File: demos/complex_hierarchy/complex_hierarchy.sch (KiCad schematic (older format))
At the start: 10 parts, among them P1 CONN_2, P2 CONN_2, U1 ICL7660, U2 78L05

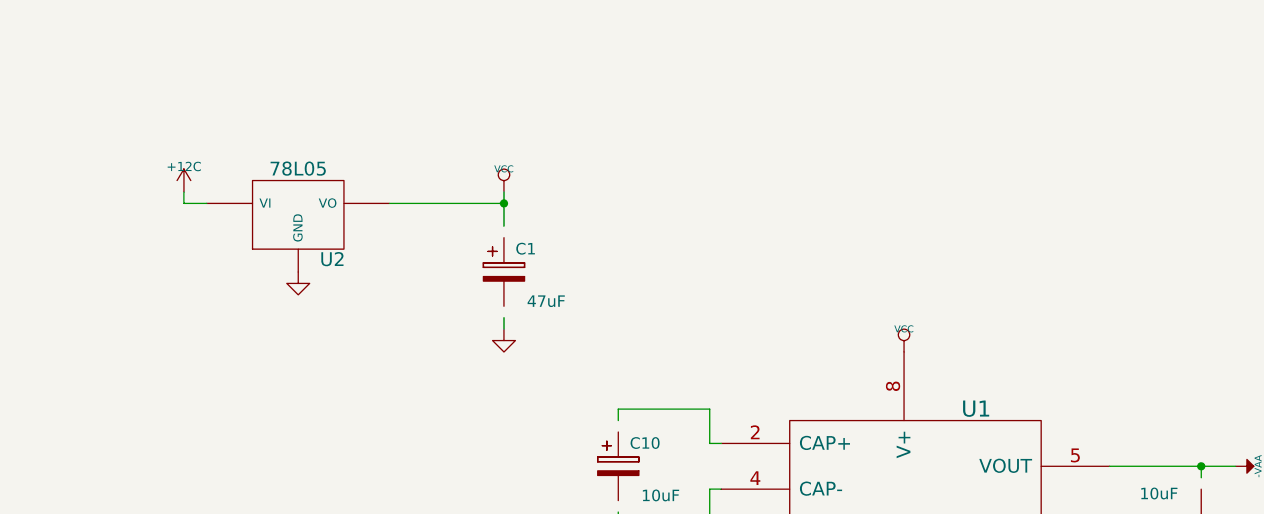
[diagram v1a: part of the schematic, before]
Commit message: Update demo files. A minor code cleaning.
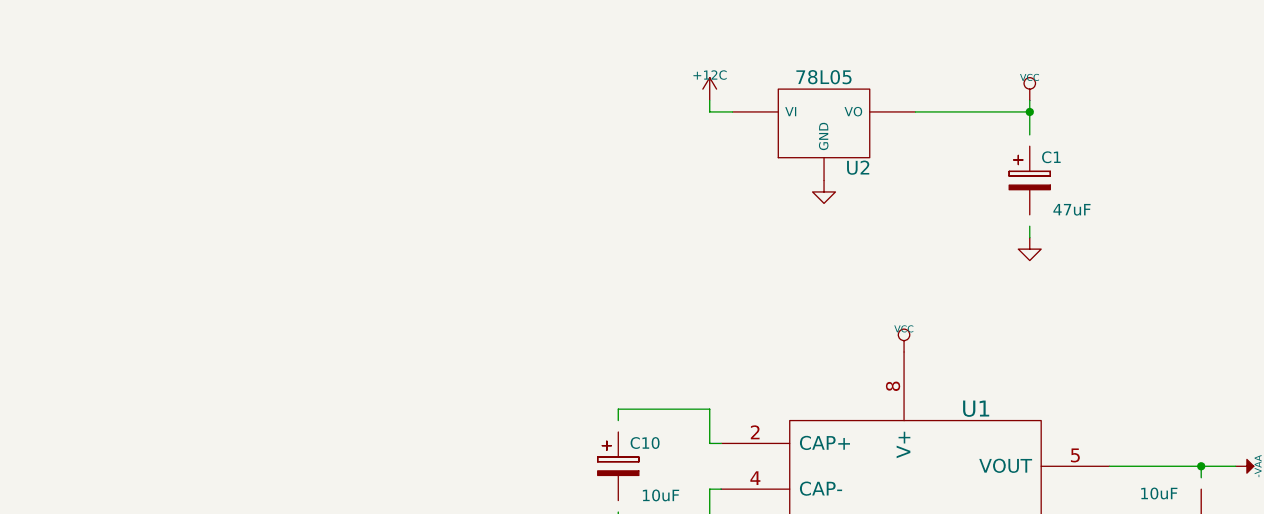
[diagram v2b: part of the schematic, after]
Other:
- moved on the sheet: C1, U2

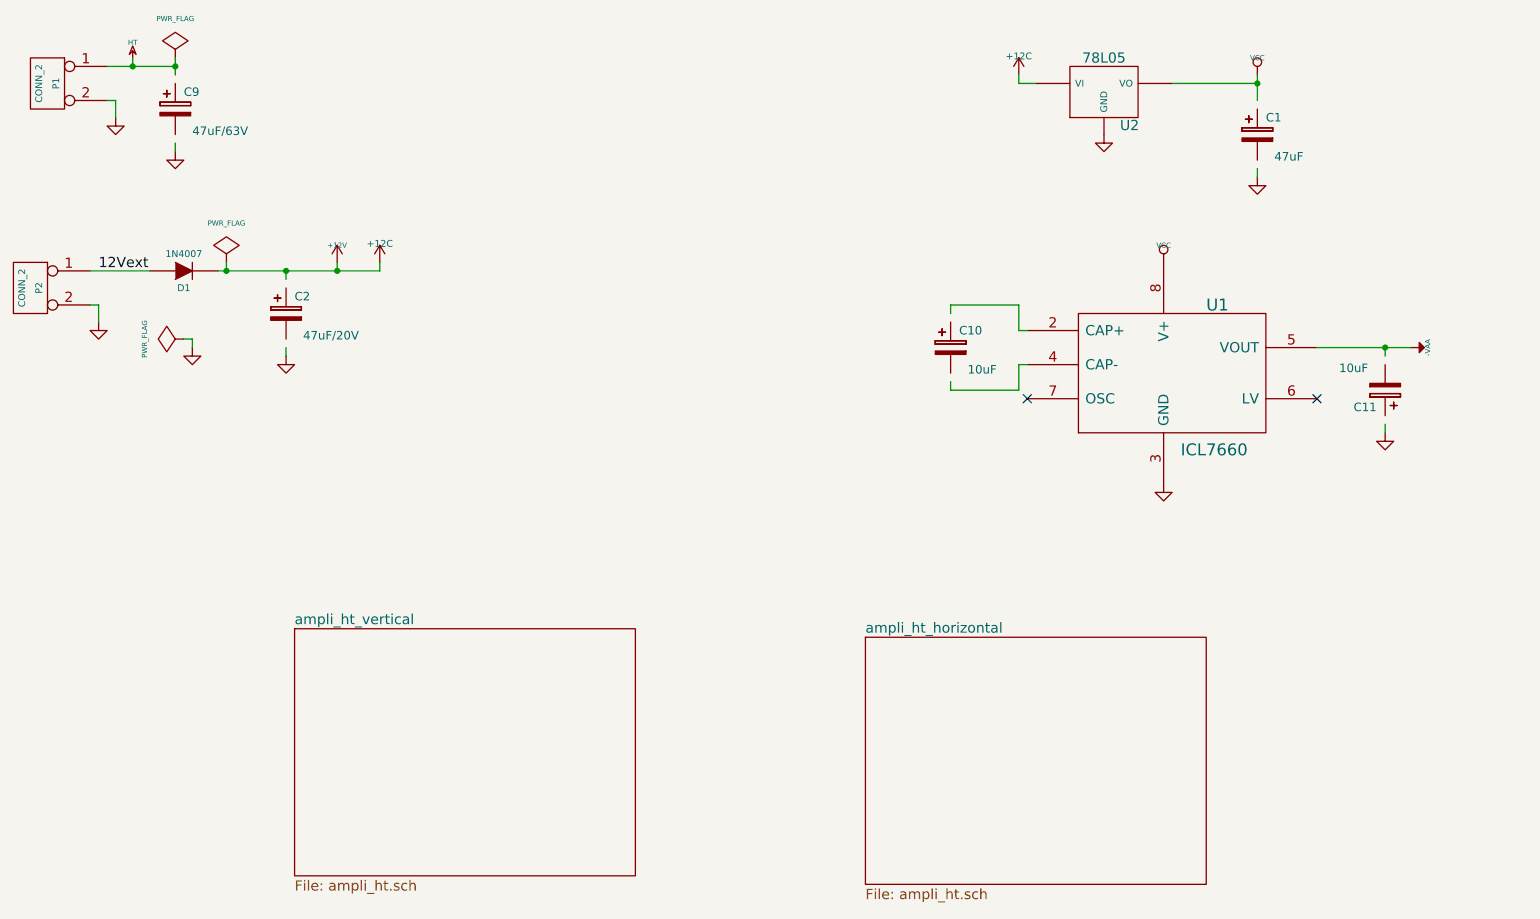
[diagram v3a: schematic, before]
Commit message: demos/ schematic tidying
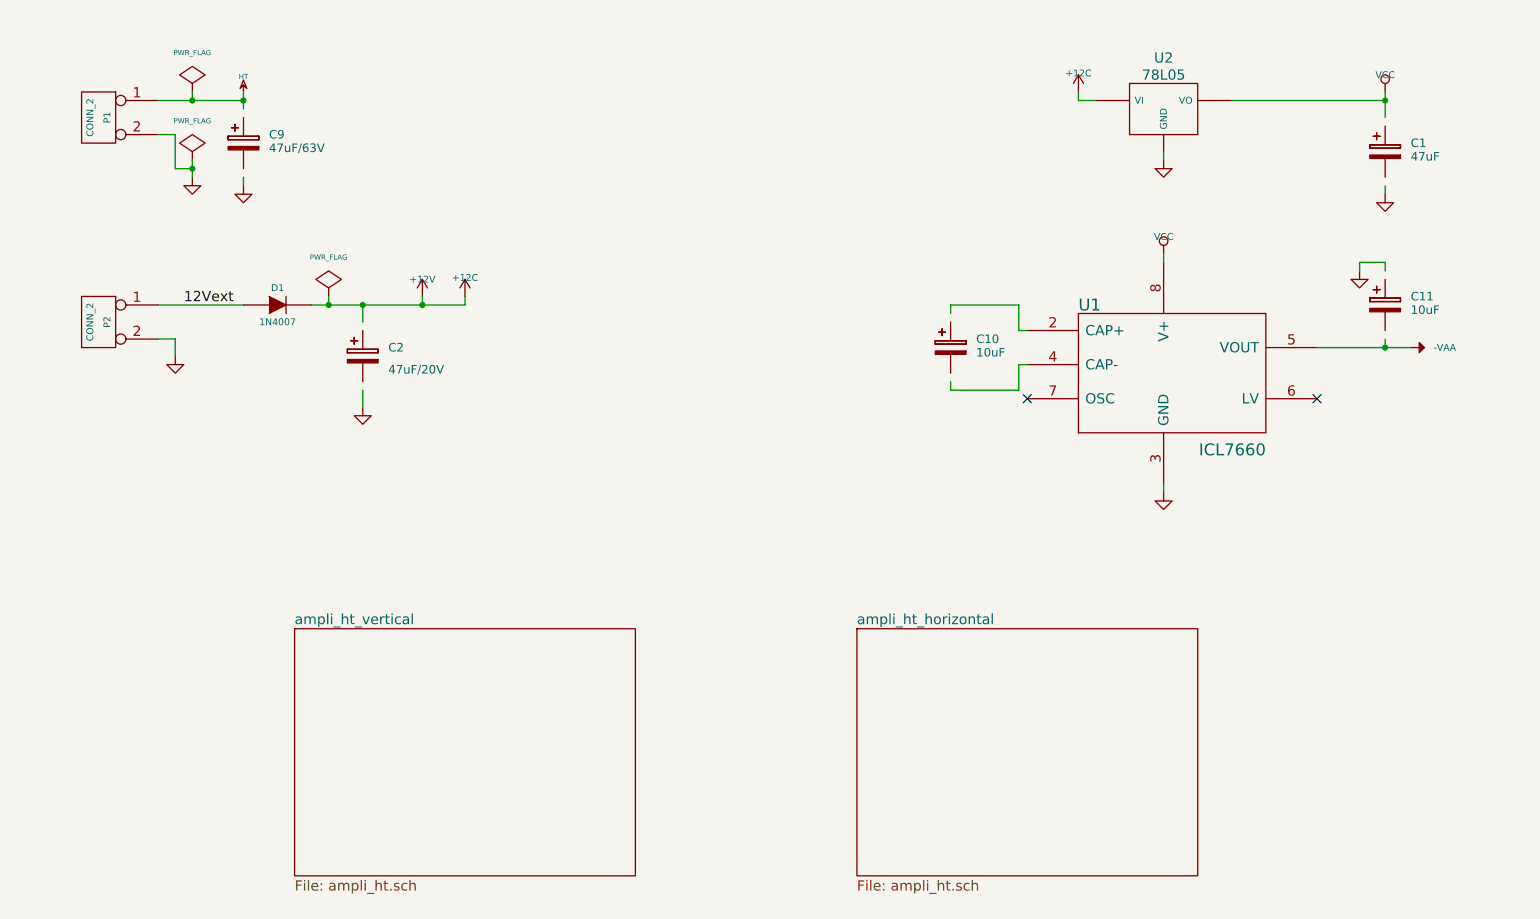
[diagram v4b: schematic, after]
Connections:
- wire segments 33 -> 38
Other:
- moved on the sheet: C1, C11, C2, C9, D1, P1, P2, U2

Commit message: Eeschema: BOM dialog: fix some minor issues when displaying messages. Cvpcb: fix Bug #1470201 (select next/previous unlinked comp and clear links not working well) demo/complex_hierarchy: use our new schematic symbols.
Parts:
- C1, C10, C11, C2: footprint (none) -> discret:CP6
- C9: footprint (none) -> discret:CP8
- D1: footprint (none) -> discret:D5; symbol DIODE -> D_Small
- P1, P2: footprint (none) -> connect:bornier2
- U1: footprint (none) -> dip_sockets:DIP-8__300_ELL
- U2: footprint (none) -> discret:LM78LXX
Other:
- moved on the sheet: C2, C9
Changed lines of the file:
@@
 EESchema Schematic File Version 2
-LIBS:complex_hierarchy_schlib
+LIBS:device
 LIBS:power
 LIBS:complex_hierarchy-cache
@@
 Connection ~ 9200 2750
 Wire Wire Line
-	9200 2700 9200 2750
-Wire Wire Line
-	6650 2950 6650 3000
+	9200 2650 9200 2750
+Wire Wire Line
+	6650 2900 6650 3000
 Wire Wire Line
 	6650 3000 7050 3000
@@
 	7050 2850 7100 2850
 Wire Wire Line
-	9200 2300 9200 2250
+	9200 2350 9200 2250
 Connection ~ 2500 1300
 Wire Wire Line
 	8300 1300 9200 1300
 Wire Wire Line
-	2900 2500 3800 2500
+	2800 2500 3800 2500
 Wire Wire Line
 	2500 1250 2500 1350
@@
 	2100 2700 2000 2700
 Wire Wire Line
-	2000 2500 2500 2500
-Wire Wire Line
-	3200 3000 3200 3100
+	2000 2500 2600 2500
+Wire Wire Line
+	3200 2900 3200 3000
 Wire Wire Line
 	3200 2500 3200 2600
@@
 	7400 1300 7500 1300
 Wire Wire Line
-	9200 1800 9200 1850
-Wire Wire Line
-	9200 1250 9200 1400
+	9200 1750 9200 1800
+Wire Wire Line
+	9200 1250 9200 1450
 Connection ~ 9200 1300
 Wire Wire Line
 	2200 1650 2200 1750
 Wire Wire Line
-	2500 1750 2500 1800
-Wire Wire Line
-	6650 2550 6650 2500
+	2500 1650 2500 1700
+Wire Wire Line
+	6650 2600 6650 2500
 Wire Wire Line
 	6650 2500 7050 2500
@@
 F 0 "C10" H 6800 2800 50  0000 L CNN
 F 1 "10uF" H 6800 2750 50  0000 L TNN
-F 2 "" H 6650 2750 60  0001 C CNN
+F 2 "discret:CP6" H 6650 2750 60  0001 C CNN
 F 3 "" H 6650 2750 60  0001 C CNN
 	1    6650 2750
@@
 F 0 "C11" H 9350 2550 50  0000 L CNN
 F 1 "10uF" H 9350 2500 50  0000 L TNN
-F 2 "" H 9200 2500 60  0001 C CNN
+F 2 "discret:CP6" H 9200 2500 60  0001 C CNN
 F 3 "" H 9200 2500 60  0001 C CNN
 	1    9200 2500
@@
 F 0 "U2" H 7900 1650 60  0000 C CNN
 F 1 "78L05" H 7900 1550 60  0000 C CNN
-F 2 "" H 7900 1350 60  0001 C CNN
+F 2 "discret:LM78LXX" H 7900 1350 60  0001 C CNN
 F 3 "" H 7900 1350 60  0001 C CNN
 	1    7900 1350
@@
 F 0 "U1" H 7400 3300 70  0000 L CNN
 F 1 "ICL7660" H 8500 2450 70  0000 R CNN
-F 2 "" H 7950 2900 60  0001 C CNN
+F 2 "dip_sockets:DIP-8__300_ELL" H 7950 2900 60  0001 C CNN
 F 3 "" H 7950 2900 60  0001 C CNN
 	1    7950 2900
@@
 L CP C9
 U 1 1 4B3A1558
-P 2500 1550
-F 0 "C9" H 2650 1600 50  0000 L CNN
-F 1 "47uF/63V" H 2650 1550 50  0000 L TNN
-F 2 "" H 2500 1550 60  0001 C CNN
-F 3 "" H 2500 1550 60  0001 C CNN
-	1    2500 1550
+P 2500 1500
+F 0 "C9" H 2650 1550 50  0000 L CNN
+F 1 "47uF/63V" H 2650 1500 50  0000 L TNN
+F 2 "discret:CP8" H 2500 1500 60  0001 C CNN
+F 3 "" H 2500 1500 60  0001 C CNN
+	1    2500 1500
 	1    0    0    -1
 $EndComp
@@
 L GND #PWR06
 U 1 1 4B3A1557
-P 2500 1800
-F 0 "#PWR06" H 2500 1800 30  0001 C CNN
-F 1 "GND" H 2500 1730 30  0001 C CNN
-F 2 "" H 2500 1800 60  0001 C CNN
-F 3 "" H 2500 1800 60  0001 C CNN
-	1    2500 1800
+P 2500 1700
+F 0 "#PWR06" H 2500 1700 30  0001 C CNN
+F 1 "GND" H 2500 1630 30  0001 C CNN
+F 2 "" H 2500 1700 60  0001 C CNN
+F 3 "" H 2500 1700 60  0001 C CNN
+	1    2500 1700
 	1    0    0    -1
 $EndComp
@@
 F 0 "P1" V 1600 1400 40  0000 C CNN
 F 1 "CONN_2" V 1700 1400 40  0000 C CNN
-F 2 "" H 1650 1400 60  0001 C CNN
+F 2 "connect:bornier2" H 1650 1400 60  0001 C CNN
 F 3 "" H 1650 1400 60  0001 C CNN
 	1    1650 1400
@@
 F 0 "C1" H 9350 1650 50  0000 L CNN
 F 1 "47uF" H 9350 1600 50  0000 L TNN
-F 2 "" H 9200 1600 60  0001 C CNN
+F 2 "discret:CP6" H 9200 1600 60  0001 C CNN
 F 3 "" H 9200 1600 60  0001 C CNN
 	1    9200 1600
@@
 L GND #PWR09
 U 1 1 4B03CEC1
-P 9200 1850
-F 0 "#PWR09" H 9200 1850 30  0001 C CNN
-F 1 "GND" H 9200 1780 30  0001 C CNN
-F 2 "" H 9200 1850 60  0001 C CNN
-F 3 "" H 9200 1850 60  0001 C CNN
-	1    9200 1850
+P 9200 1800
+F 0 "#PWR09" H 9200 1800 30  0001 C CNN
+F 1 "GND" H 9200 1730 30  0001 C CNN
+F 2 "" H 9200 1800 60  0001 C CNN
+F 3 "" H 9200 1800 60  0001 C CNN
+	1    9200 1800
 	1    0    0    -1
 $EndComp
@@
 L GND #PWR017
 U 1 1 4AE173D0
-P 3200 3100
-F 0 "#PWR017" H 3200 3100 30  0001 C CNN
-F 1 "GND" H 3200 3030 30  0001 C CNN
-F 2 "" H 3200 3100 60  0001 C CNN
-F 3 "" H 3200 3100 60  0001 C CNN
-	1    3200 3100
+P 3200 3000
+F 0 "#PWR017" H 3200 3000 30  0001 C CNN
+F 1 "GND" H 3200 2930 30  0001 C CNN
+F 2 "" H 3200 3000 60  0001 C CNN
+F 3 "" H 3200 3000 60  0001 C CNN
+	1    3200 3000
 	1    0    0    -1
 $EndComp
@@
 L CP C2
 U 1 1 4AE173CF
-P 3200 2800
-F 0 "C2" H 3350 2850 50  0000 L CNN
-F 1 "47uF/20V" H 3350 2750 50  0000 L TNN
-F 2 "" H 3200 2800 60  0001 C CNN
-F 3 "" H 3200 2800 60  0001 C CNN
-	1    3200 2800
-	1    0    0    -1
-$EndComp
-$Comp
-L DIODE D1
+P 3200 2750
+F 0 "C2" H 3350 2800 50  0000 L CNN
+F 1 "47uF/20V" H 3350 2700 50  0000 L TNN
+F 2 "discret:CP6" H 3200 2750 60  0001 C CNN
+F 3 "" H 3200 2750 60  0001 C CNN
+	1    3200 2750
+	1    0    0    -1
+$EndComp
+$Comp
+L D_Small D1
 U 1 1 4AE172F4
 P 2700 2500
 F 0 "D1" H 2700 2400 40  0000 C CNN
 F 1 "1N4007" H 2700 2600 40  0000 C CNN
-F 2 "" H 2700 2500 60  0001 C CNN
+F 2 "discret:D5" H 2700 2500 60  0001 C CNN
 F 3 "" H 2700 2500 60  0001 C CNN
 	1    2700 2500
-	1    0    0    1
+	-1   0    0    -1
 $EndComp
 $Comp
@@
 F 0 "P2" V 1600 2600 40  0000 C CNN
 F 1 "CONN_2" V 1700 2600 40  0000 C CNN
-F 2 "" H 1650 2600 60  0001 C CNN
+F 2 "connect:bornier2" H 1650 2600 60  0001 C CNN
 F 3 "" H 1650 2600 60  0001 C CNN
 	1    1650 2600

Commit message: polygons in footprint body: fix incorrect calculation of polygons with clearance or outline thickness (fix bug #1511366) Clean demos
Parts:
- C1, C10, C11, C2: footprint discret:CP6 -> Discret:CP6
- C9: footprint discret:CP8 -> Discret:CP8
- D1: footprint discret:D5 -> Discret:D5
- P1, P2: footprint connect:bornier2 -> Connect:bornier2
- U2: footprint discret:LM78LXX -> Discret:LM78LXX
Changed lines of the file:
@@
 EESchema Schematic File Version 2
-LIBS:device
 LIBS:power
+LIBS:complex_hierarchy_schlib
 LIBS:complex_hierarchy-cache
 EELAYER 25 0
@@
 F 0 "C10" H 6800 2800 50  0000 L CNN
 F 1 "10uF" H 6800 2750 50  0000 L TNN
-F 2 "discret:CP6" H 6650 2750 60  0001 C CNN
+F 2 "Discret:CP6" H 6650 2750 60  0001 C CNN
 F 3 "" H 6650 2750 60  0001 C CNN
 	1    6650 2750
@@
 F 0 "C11" H 9350 2550 50  0000 L CNN
 F 1 "10uF" H 9350 2500 50  0000 L TNN
-F 2 "discret:CP6" H 9200 2500 60  0001 C CNN
+F 2 "Discret:CP6" H 9200 2500 60  0001 C CNN
 F 3 "" H 9200 2500 60  0001 C CNN
 	1    9200 2500
@@
 F 0 "U2" H 7900 1650 60  0000 C CNN
 F 1 "78L05" H 7900 1550 60  0000 C CNN
-F 2 "discret:LM78LXX" H 7900 1350 60  0001 C CNN
+F 2 "Discret:LM78LXX" H 7900 1350 60  0001 C CNN
 F 3 "" H 7900 1350 60  0001 C CNN
 	1    7900 1350
@@
 F 0 "C9" H 2650 1550 50  0000 L CNN
 F 1 "47uF/63V" H 2650 1500 50  0000 L TNN
-F 2 "discret:CP8" H 2500 1500 60  0001 C CNN
+F 2 "Discret:CP8" H 2500 1500 60  0001 C CNN
 F 3 "" H 2500 1500 60  0001 C CNN
 	1    2500 1500
@@
 F 0 "P1" V 1600 1400 40  0000 C CNN
 F 1 "CONN_2" V 1700 1400 40  0000 C CNN
-F 2 "connect:bornier2" H 1650 1400 60  0001 C CNN
+F 2 "Connect:bornier2" H 1650 1400 60  0001 C CNN
 F 3 "" H 1650 1400 60  0001 C CNN
 	1    1650 1400
@@
 F 0 "C1" H 9350 1650 50  0000 L CNN
 F 1 "47uF" H 9350 1600 50  0000 L TNN
-F 2 "discret:CP6" H 9200 1600 60  0001 C CNN
+F 2 "Discret:CP6" H 9200 1600 60  0001 C CNN
 F 3 "" H 9200 1600 60  0001 C CNN
 	1    9200 1600
@@
 F 0 "C2" H 3350 2800 50  0000 L CNN
 F 1 "47uF/20V" H 3350 2700 50  0000 L TNN
-F 2 "discret:CP6" H 3200 2750 60  0001 C CNN
+F 2 "Discret:CP6" H 3200 2750 60  0001 C CNN
 F 3 "" H 3200 2750 60  0001 C CNN
 	1    3200 2750
@@
 F 0 "D1" H 2700 2400 40  0000 C CNN
 F 1 "1N4007" H 2700 2600 40  0000 C CNN
-F 2 "discret:D5" H 2700 2500 60  0001 C CNN
+F 2 "Discret:D5" H 2700 2500 60  0001 C CNN
 F 3 "" H 2700 2500 60  0001 C CNN
 	1    2700 2500
@@
 F 0 "P2" V 1600 2600 40  0000 C CNN
 F 1 "CONN_2" V 1700 2600 40  0000 C CNN
-F 2 "connect:bornier2" H 1650 2600 60  0001 C CNN
+F 2 "Connect:bornier2" H 1650 2600 60  0001 C CNN
 F 3 "" H 1650 2600 60  0001 C CNN
 	1    1650 2600

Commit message: merge from production git:004ca3c 16.01.2017
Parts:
- U1: footprint dip_sockets:DIP-8__300_ELL -> Housings_DIP:DIP-8_W7.62mm_LongPads
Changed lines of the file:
@@
 LIBS:complex_hierarchy_schlib
 LIBS:complex_hierarchy-cache
-EELAYER 25 0
+EELAYER 26 0
 EELAYER END
 $Descr A4 11693 8268
 encoding utf-8
 Sheet 1 3
-Title ""
-Date "21 mar 2015"
+Title "Complex hierarchy: demo"
+Date "2017-01-15"
 Rev ""
 Comp ""
@@
 F 0 "C10" H 6800 2800 50  0000 L CNN
 F 1 "10uF" H 6800 2750 50  0000 L TNN
-F 2 "Discret:CP6" H 6650 2750 60  0001 C CNN
+F 2 "Discret:CP6" H 6850 2650 30  0000 C CNN
 F 3 "" H 6650 2750 60  0001 C CNN
 	1    6650 2750
@@
 F 0 "C11" H 9350 2550 50  0000 L CNN
 F 1 "10uF" H 9350 2500 50  0000 L TNN
-F 2 "Discret:CP6" H 9200 2500 60  0001 C CNN
+F 2 "Discret:CP6" H 9550 2400 30  0000 C CNN
 F 3 "" H 9200 2500 60  0001 C CNN
 	1    9200 2500
@@
 F 0 "U2" H 7900 1650 60  0000 C CNN
 F 1 "78L05" H 7900 1550 60  0000 C CNN
-F 2 "Discret:LM78LXX" H 7900 1350 60  0001 C CNN
+F 2 "Discret:LM78LXX" H 8100 1150 30  0000 C CNN
 F 3 "" H 7900 1350 60  0001 C CNN
 	1    7900 1350
@@
 F 0 "U1" H 7400 3300 70  0000 L CNN
 F 1 "ICL7660" H 8500 2450 70  0000 R CNN
-F 2 "dip_sockets:DIP-8__300_ELL" H 7950 2900 60  0001 C CNN
+F 2 "Housings_DIP:DIP-8_W7.62mm_LongPads" H 8950 2300 60  0000 C CNN
 F 3 "" H 7950 2900 60  0001 C CNN
 	1    7950 2900
@@
 F 0 "C9" H 2650 1550 50  0000 L CNN
 F 1 "47uF/63V" H 2650 1500 50  0000 L TNN
-F 2 "Discret:CP8" H 2500 1500 60  0001 C CNN
+F 2 "Discret:CP8" H 2800 1400 30  0000 C CNN
 F 3 "" H 2500 1500 60  0001 C CNN
 	1    2500 1500
@@
 F 0 "P1" V 1600 1400 40  0000 C CNN
 F 1 "CONN_2" V 1700 1400 40  0000 C CNN
-F 2 "Connect:bornier2" H 1650 1400 60  0001 C CNN
+F 2 "Connect:bornier2" H 1650 1200 30  0000 C CNN
 F 3 "" H 1650 1400 60  0001 C CNN
 	1    1650 1400
@@
 F 0 "C1" H 9350 1650 50  0000 L CNN
 F 1 "47uF" H 9350 1600 50  0000 L TNN
-F 2 "Discret:CP6" H 9200 1600 60  0001 C CNN
+F 2 "Discret:CP6" H 9500 1500 30  0000 C CNN
 F 3 "" H 9200 1600 60  0001 C CNN
 	1    9200 1600
@@
 F 0 "C2" H 3350 2800 50  0000 L CNN
 F 1 "47uF/20V" H 3350 2700 50  0000 L TNN
-F 2 "Discret:CP6" H 3200 2750 60  0001 C CNN
+F 2 "Discret:CP6" H 3550 2600 30  0000 C CNN
 F 3 "" H 3200 2750 60  0001 C CNN
 	1    3200 2750
@@
 F 0 "D1" H 2700 2400 40  0000 C CNN
 F 1 "1N4007" H 2700 2600 40  0000 C CNN
-F 2 "Discret:D5" H 2700 2500 60  0001 C CNN
+F 2 "Discret:D5" H 2700 2350 30  0000 C CNN
 F 3 "" H 2700 2500 60  0001 C CNN
 	1    2700 2500
@@
 F 0 "P2" V 1600 2600 40  0000 C CNN
 F 1 "CONN_2" V 1700 2600 40  0000 C CNN
-F 2 "Connect:bornier2" H 1650 2600 60  0001 C CNN
+F 2 "Connect:bornier2" H 1650 2400 30  0000 C CNN
 F 3 "" H 1650 2600 60  0001 C CNN
 	1    1650 2600
